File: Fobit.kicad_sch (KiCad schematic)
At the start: 9 parts, among them U1 nRF52840, U2 NPM1100-QDAA-R

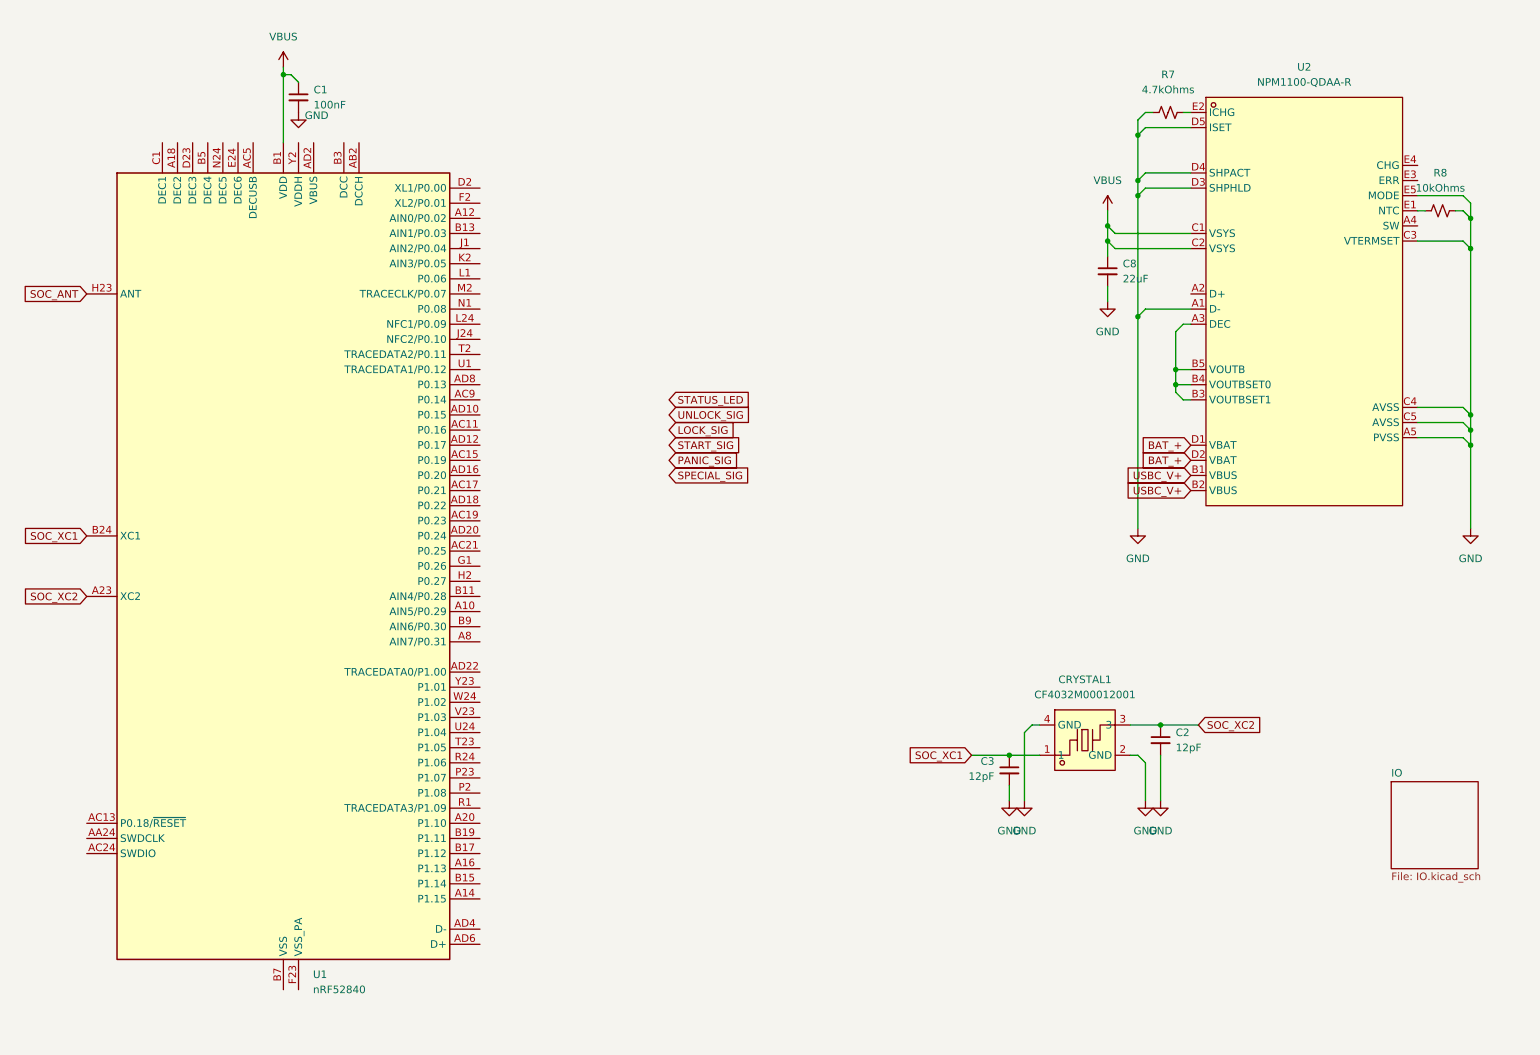
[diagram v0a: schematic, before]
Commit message: Corrected USB host/slave resistors. Added REG1 DC-DC stage. Removed X2, added X1.
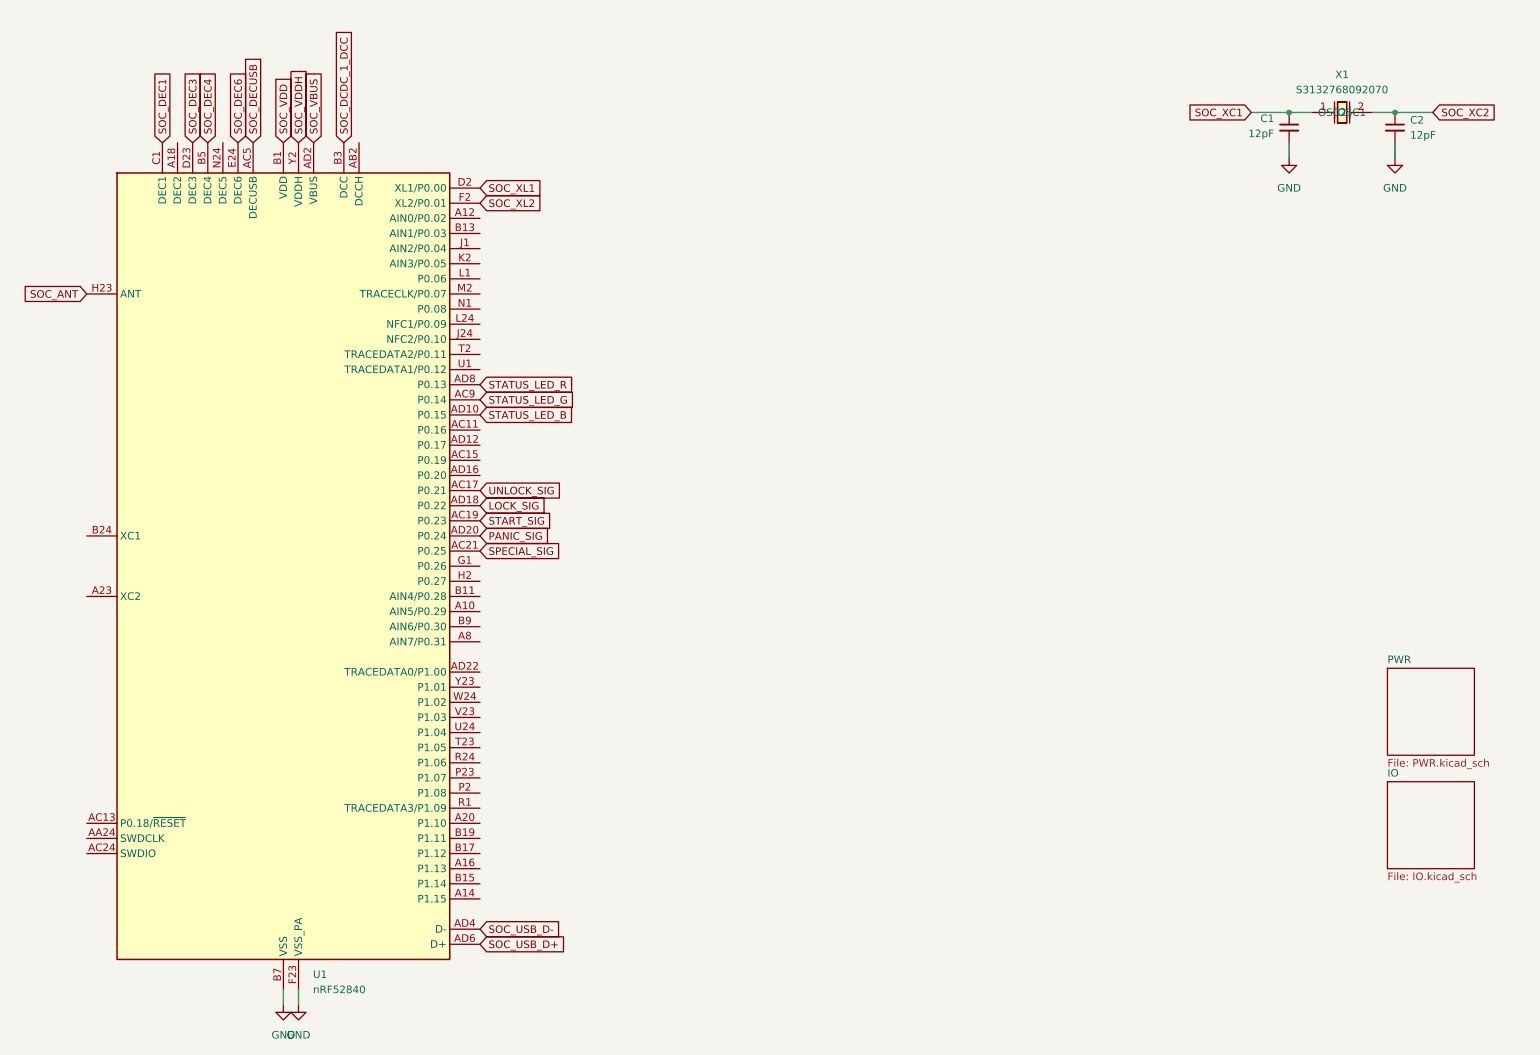
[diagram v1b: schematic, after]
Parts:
- removed C1: 100nF, Capacitor_SMD:C_0402_1005Metric_Pad0.74x0.62mm_HandSolder, symbol Device:C_Small
- removed C8: 22uF, Capacitor_SMD:C_0402_1005Metric_Pad0.74x0.62mm_HandSolder, symbol Device:C_Small
- removed CRYSTAL1: CF4032M00012001, easyeda2kicad:CRYSTAL-SMD_4P-L3.2-W2.5-BL_SIT8008BI, symbol easyeda2kicad:CF4032M00012001
- removed R7: 4.7kOhms, Resistor_SMD:R_0402_1005Metric_Pad0.72x0.64mm_HandSolder, symbol Device:R_Small_US
- removed R8: 10kOhms, Resistor_SMD:R_0402_1005Metric_Pad0.72x0.64mm_HandSolder, symbol Device:R_Small_US
- removed U2: NPM1100-QDAA-R, easyeda2kicad:WLCSP-25_L2.1-W2.1-R5-C5-P0.40-TL-1, symbol easyeda2kicad:NPM1100-CAAA-E-R7
- added X1: S3132768092070, MyLib:OSC-SMD_2P-L3.2-W1.5, symbol MySymbols:S3132768092070
- C1: renamed from C3; footprint Capacitor_SMD:C_0402_1005Metric_Pad0.74x0.62mm_HandSolder -> FobitLib:C_0402_1005Metric_Pad0.74x0.62mm_HandSolder; symbol Device:C_Small -> FobitSymbols:C_Small
- C2: footprint Capacitor_SMD:C_0402_1005Metric_Pad0.74x0.62mm_HandSolder -> FobitLib:C_0402_1005Metric_Pad0.74x0.62mm_HandSolder; symbol Device:C_Small -> FobitSymbols:C_Small
- U1: footprint Package_DFN_QFN:Nordic_AQFN-73-1EP_7x7mm_P0.5mm -> FobitLib:Nordic_AQFN-73-1EP_7x7mm_P0.5mm; symbol MCU_Nordic:nRF52840 -> FobitSymbols:nRF52840
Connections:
- net GND: now also U1.B7 (VSS), U1.EP (VSS), U1.F23 (VSS_PA)
- net LOCK_SIG: now also U1.AD18 (P0.22)
- net PANIC_SIG: now also U1.AD20 (P0.24)
- net SOC_XC1: now also X1.1 (OSC1); no longer U1.B24 (XC1)
- net SOC_XC2: now also X1.2 (OSC2); no longer U1.A23 (XC2)
- net SPECIAL_SIG: now also U1.AC21 (P0.25)
- net START_SIG: now also U1.AC19 (P0.23)
- net UNLOCK_SIG: now also U1.AC17 (P0.21)
- net SOC_DECUSB: now reaches U1.AC5 (DECUSB)
- net STATUS_LED_G: now reaches U1.AC9 (P0.14)
- net STATUS_LED_B: now reaches U1.AD10 (P0.15)
- net SOC_VBUS: now reaches U1.AD2 (VBUS)
- net SOC_USB_D-: now reaches U1.AD4 (D-)
- net SOC_USB_D+: now reaches U1.AD6 (D+)
- net STATUS_LED_R: now reaches U1.AD8 (P0.13)
- net SOC_DCDC_1_DCC: now reaches U1.B3 (DCC)
- net SOC_DEC4: now reaches U1.B5 (DEC4)
- net SOC_DEC1: now reaches U1.C1 (DEC1)
- net SOC_XL1: now reaches U1.D2 (XL1/P0.00)
- net SOC_DEC3: now reaches U1.D23 (DEC3)
- net SOC_DEC6: now reaches U1.E24 (DEC6)
- net SOC_XL2: now reaches U1.F2 (XL2/P0.01)
- net SOC_VDDH: now reaches U1.Y2 (VDDH)
- net VBUS renamed SOC_VDD
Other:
- added sheet PWR (PWR.kicad_sch)
- moved on the sheet: C1, C2
